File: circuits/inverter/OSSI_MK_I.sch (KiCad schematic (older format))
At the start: 0 parts

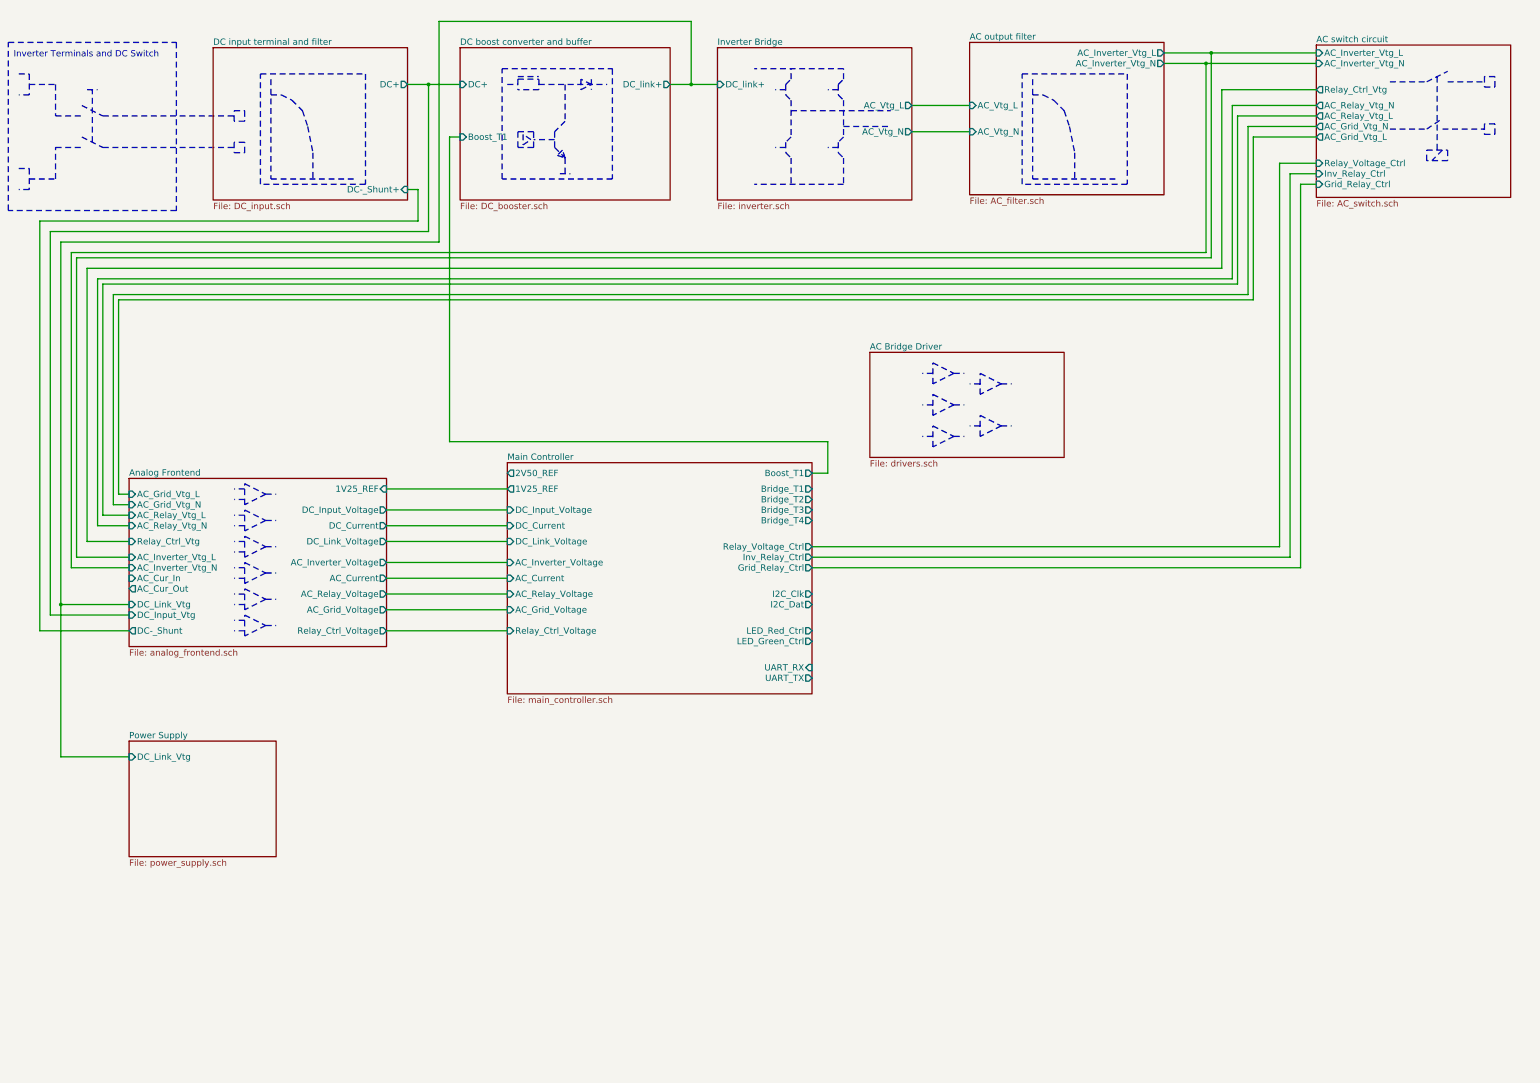
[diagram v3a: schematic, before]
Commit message: bulk-updates libraries and schematics
schematic is updated to Kicad 5.1.14
updates various sheets with new circuits
adds various component libraries
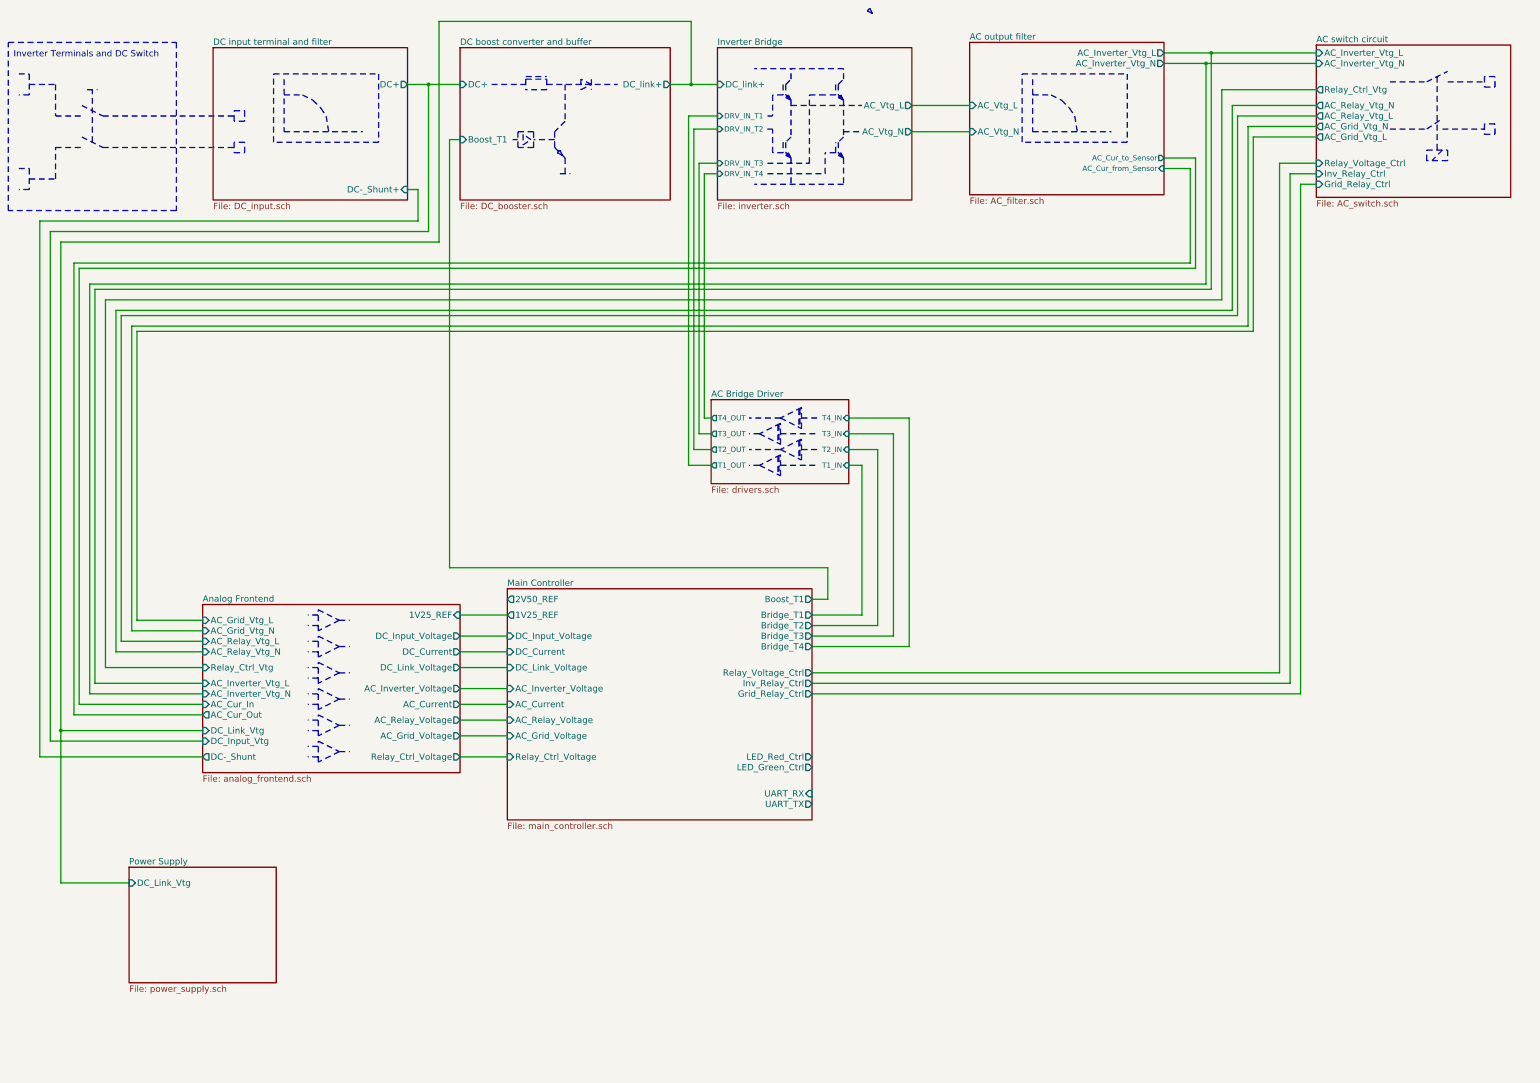
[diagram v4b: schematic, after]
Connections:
- wire segments 78 -> 117

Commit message: minor updates and cleaup
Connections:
- wire segments 117 -> 132
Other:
- note added: "15V"
- note added: "15V\n"
